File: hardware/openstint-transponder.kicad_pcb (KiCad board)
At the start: 4 copper layers, 18.5 x 15 mm, 38 parts, among them J1 V+, J2 V-, Q1 PMGD280UN, U1 ATtiny816/1616, U2 10 MHz, U3 SPX3819M5-L-3-3

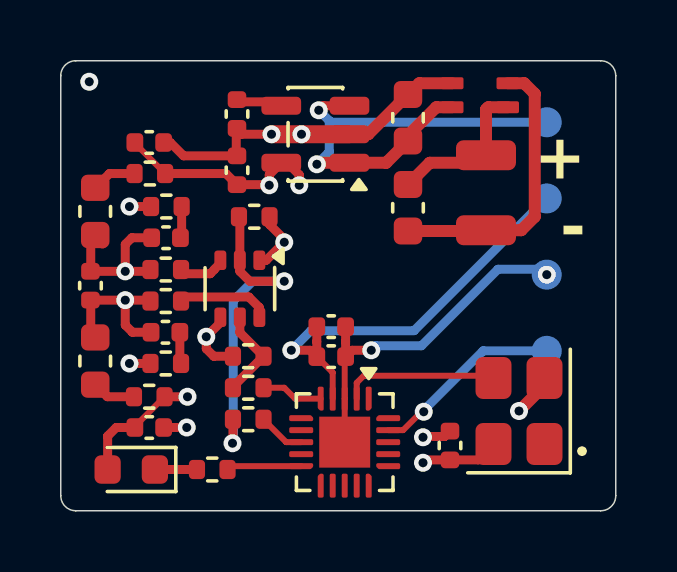
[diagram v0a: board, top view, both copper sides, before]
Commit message: use 2x tuning caps
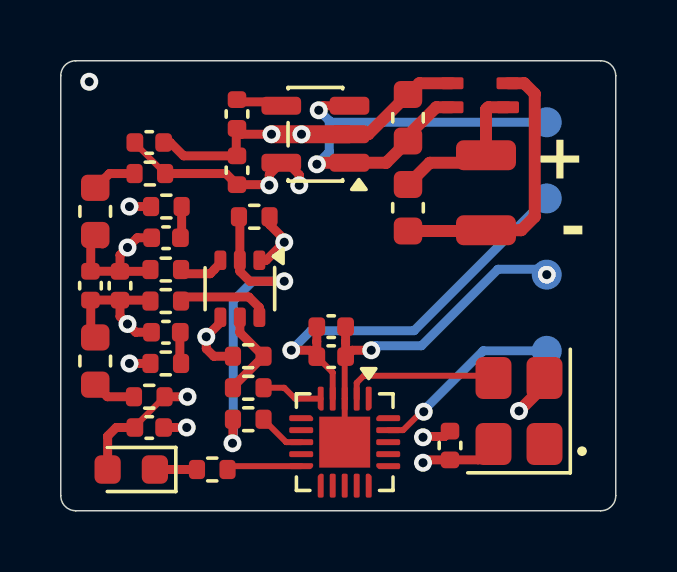
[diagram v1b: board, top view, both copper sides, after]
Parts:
- added C2: 910p/C0G, Capacitor_SMD:C_0402_1005Metric, F.Cu at (131.7, 102.5)
- C6: value 1800p/C0G -> 910p/C0G
